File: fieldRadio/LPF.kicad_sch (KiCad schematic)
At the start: 91 parts, among them K1 G5V-2, K2 G5V-2, K3 G5V-2, K4 G5V-2, K5 G5V-2, Q1 MMBT3904, Q2 MMBT3904, Q3 MMBT3904, Q4 MMBT3904, Q5 MMBT3904

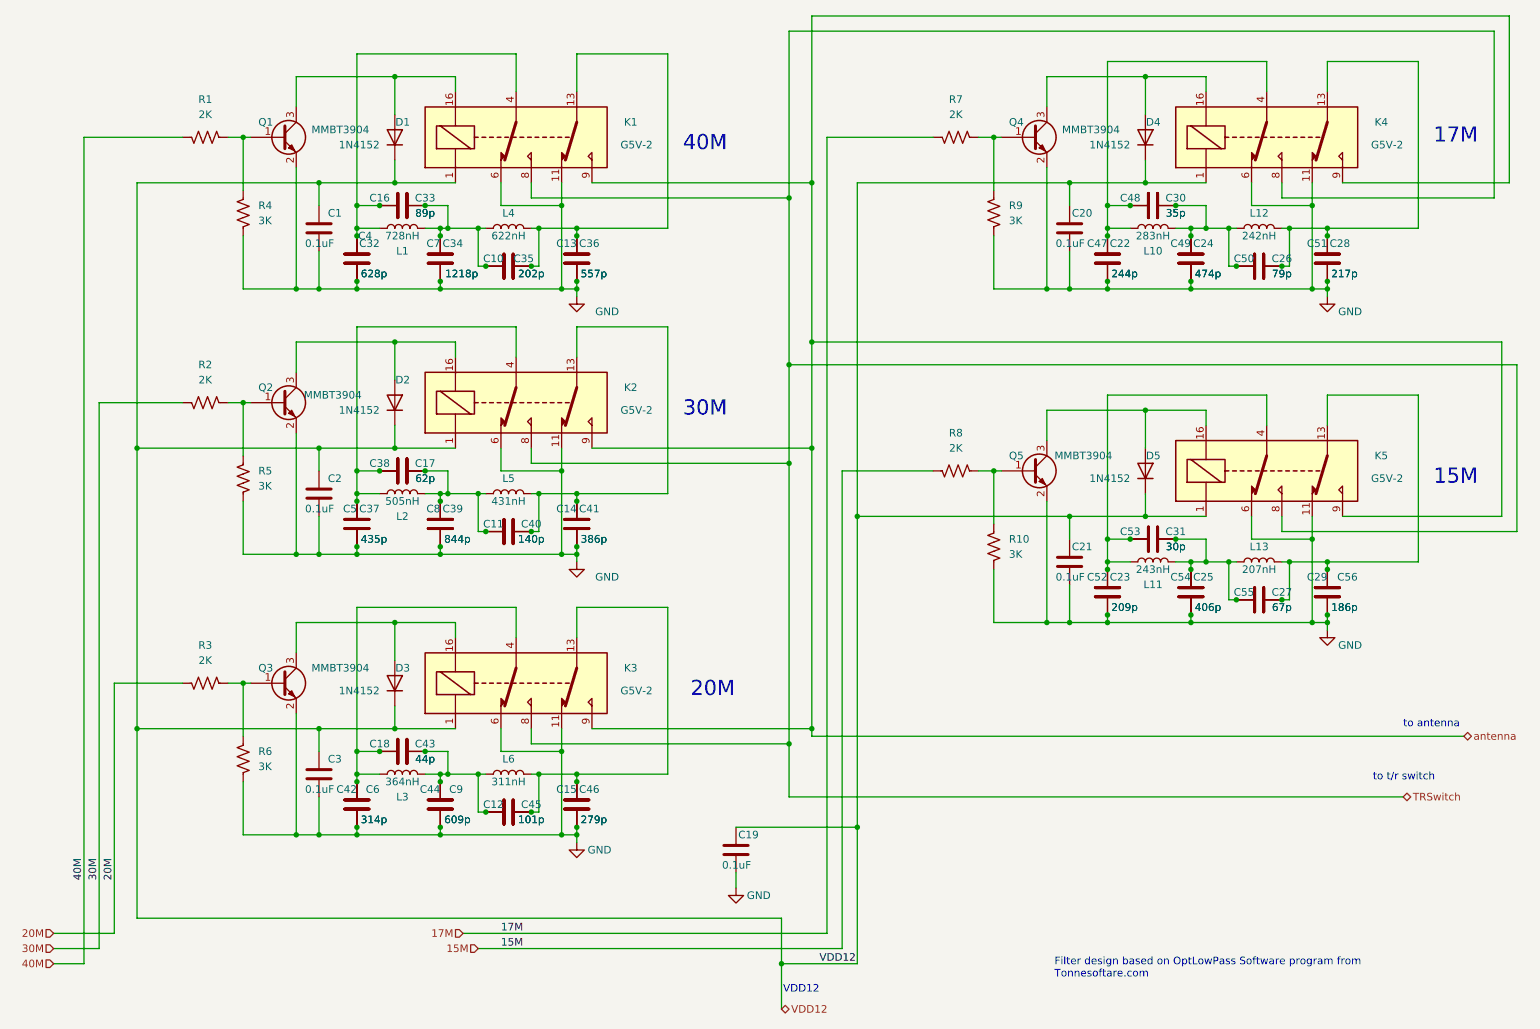
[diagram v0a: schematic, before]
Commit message: Building fieldradio schematic
in process of building field radio schematics
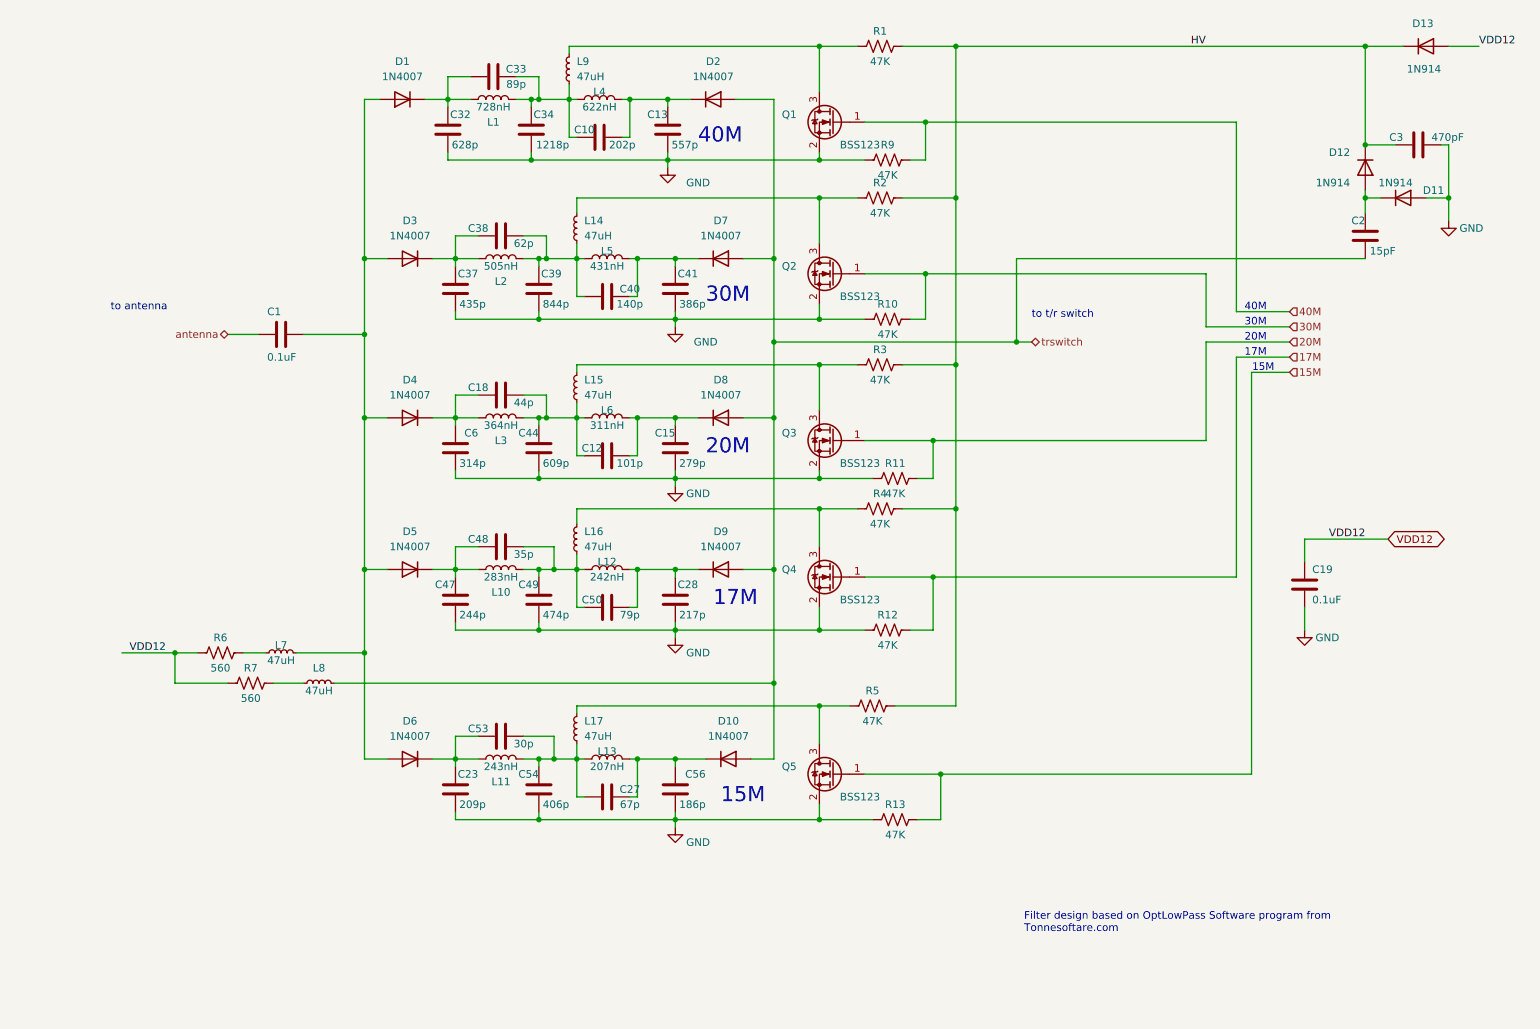
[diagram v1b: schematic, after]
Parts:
- removed C11: 140p, Capacitor_THT:C_Disc_D4.3mm_W1.9mm_P5.00mm, symbol Device:C
- removed C14: 386p, Capacitor_THT:C_Disc_D4.3mm_W1.9mm_P5.00mm, symbol Device:C
- removed C16: 89p, Capacitor_THT:C_Disc_D4.3mm_W1.9mm_P5.00mm, symbol Device:C
- removed C17: 62p, Capacitor_THT:C_Disc_D4.3mm_W1.9mm_P5.00mm, symbol Device:C
- removed C20, C21: 0.1uF, Capacitor_SMD:C_0603_1608Metric_Pad1.08x0.95mm_HandSolder, symbol Device:C
- removed C22: 244p, Capacitor_THT:C_Disc_D4.3mm_W1.9mm_P5.00mm, symbol Device:C
- removed C24: 474p, Capacitor_THT:C_Disc_D4.3mm_W1.9mm_P5.00mm, symbol Device:C
- removed C25: 406p, Capacitor_THT:C_Disc_D4.3mm_W1.9mm_P5.00mm, symbol Device:C
- removed C26: 79p, Capacitor_THT:C_Disc_D4.3mm_W1.9mm_P5.00mm, symbol Device:C
- removed C29: 186p, Capacitor_THT:C_Disc_D4.3mm_W1.9mm_P5.00mm, symbol Device:C
- removed C30: 35p, Capacitor_THT:C_Disc_D4.3mm_W1.9mm_P5.00mm, symbol Device:C
- removed C31: 30p, Capacitor_THT:C_Disc_D4.3mm_W1.9mm_P5.00mm, symbol Device:C
- removed C35: 202p, Capacitor_THT:C_Disc_D4.3mm_W1.9mm_P5.00mm, symbol Device:C
- removed C36: 557p, Capacitor_THT:C_Disc_D4.3mm_W1.9mm_P5.00mm, symbol Device:C
- removed C4: 628p, Capacitor_THT:C_Disc_D4.3mm_W1.9mm_P5.00mm, symbol Device:C
- removed C42: 314p, Capacitor_THT:C_Disc_D4.3mm_W1.9mm_P5.00mm, symbol Device:C
- removed C43: 44p, Capacitor_THT:C_Disc_D4.3mm_W1.9mm_P5.00mm, symbol Device:C
- removed C45: 101p, Capacitor_THT:C_Disc_D4.3mm_W1.9mm_P5.00mm, symbol Device:C
- removed C46: 279p, Capacitor_THT:C_Disc_D4.3mm_W1.9mm_P5.00mm, symbol Device:C
- removed C5: 435p, Capacitor_THT:C_Disc_D4.3mm_W1.9mm_P5.00mm, symbol Device:C
- removed C51: 217p, Capacitor_THT:C_Disc_D4.3mm_W1.9mm_P5.00mm, symbol Device:C
- removed C52: 209p, Capacitor_THT:C_Disc_D4.3mm_W1.9mm_P5.00mm, symbol Device:C
- removed C55: 67p, Capacitor_THT:C_Disc_D4.3mm_W1.9mm_P5.00mm, symbol Device:C
- removed C7: 1218p, Capacitor_THT:C_Disc_D4.3mm_W1.9mm_P5.00mm, symbol Device:C
- removed C8: 844p, Capacitor_THT:C_Disc_D4.3mm_W1.9mm_P5.00mm, symbol Device:C
- removed C9: 609p, Capacitor_THT:C_Disc_D4.3mm_W1.9mm_P5.00mm, symbol Device:C
- removed D1, D2, D3, D4, D5: 1N4152, Diode_THT:D_DO-41_SOD81_P7.62mm_Horizontal, symbol Device:D
- removed K1, K2, K3, K4, K5: G5V-2, Relay_THT:Relay_DPDT_Omron_G5V-2, symbol Relay:G5V-2
- removed Q1, Q2, Q3, Q4, Q5: MMBT3904, Package_TO_SOT_SMD:SOT-23, symbol Device:Q_NPN_BEC
- removed R8: 2K, Resistor_SMD:R_0603_1608Metric_Pad0.98x0.95mm_HandSolder, symbol Device:R_US
- added D1, D10, D2, D3, D4, D5, D6, D7, D8, D9: 1N4007, Diode_THT:D_DO-41_SOD81_P10.16mm_Horizontal, symbol Diode:1N4007
- added D11, D12, D13: 1N914, Diode_THT:D_DO-35_SOD27_P7.62mm_Horizontal, symbol Diode:1N914
- added L14, L15, L16, L17, L7, L8, L9: 47uH, Inductor_THT:L_Axial_L11.0mm_D4.5mm_P7.62mm_Vertical_Fastron_MECC, symbol Device:L_Small
- added Q1, Q2, Q3, Q4, Q5: BSS123, Package_TO_SOT_SMD:SOT-23-3, symbol Device:Q_NMOS_GSD
- added R11, R12, R13: 47K, Resistor_SMD:R_0603_1608Metric_Pad0.98x0.95mm_HandSolder, symbol Device:R_US
- C1: footprint Capacitor_SMD:C_0603_1608Metric_Pad1.08x0.95mm_HandSolder -> Capacitor_THT:C_Disc_D4.3mm_W1.9mm_P5.00mm
- C10, C12, C13, C15, C18, C23, C27, C28, C32, C33, C34, C37, C38, C39, C40, C41, C44, C47, C48, C49, C50, C53, C54, C56, C6: footprint Capacitor_THT:C_Disc_D4.3mm_W1.9mm_P5.00mm -> Capacitor_SMD:C_1206_3216Metric_Pad1.33x1.80mm_HandSolder
- C2: value 0.1uF -> 15pF; footprint Capacitor_SMD:C_0603_1608Metric_Pad1.08x0.95mm_HandSolder -> Capacitor_THT:C_Disc_D4.3mm_W1.9mm_P5.00mm
- C3: value 0.1uF -> 470pF; footprint Capacitor_SMD:C_0603_1608Metric_Pad1.08x0.95mm_HandSolder -> Capacitor_THT:C_Disc_D4.3mm_W1.9mm_P5.00mm
- R1, R2, R3: value 2K -> 47K
- R10, R4, R5, R9: value 3K -> 47K
- R6: value 3K -> 560; footprint Resistor_SMD:R_0603_1608Metric_Pad0.98x0.95mm_HandSolder -> Resistor_THT:R_Axial_DIN0617_L17.0mm_D6.0mm_P20.32mm_Horizontal
- R7: value 2K -> 560; footprint Resistor_SMD:R_0603_1608Metric_Pad0.98x0.95mm_HandSolder -> Resistor_THT:R_Axial_DIN0617_L17.0mm_D6.0mm_P20.32mm_Horizontal
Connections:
- net 15M: now also Q5.1 (G), R13.2
- net 17M: now also Q4.1 (G), R12.2; no longer R7.2
- net 20M: now also Q3.1 (G), R11.2; no longer R3.2
- net 30M: now also R10.2, Q2.1 (G); no longer R2.2
- net 40M: now also R9.2, Q1.1 (G); no longer R1.2
- net GND: now also C19.1, R10.1, R9.1, D11.2 (A), Q1.2 (S), Q2.2 (S), Q3.2 (S), Q4.2 (S), Q5.2 (S), R11.1, R12.1, R13.1; no longer C1.2, C19.2, C2.2, R10.2, R4.2, R5.2, R6.2, R9.2
- net VDD12: now also C19.2, R6.1, R7.1, D13.2 (A); no longer C1.1, C19.1, C2.1, C3.1
- net antenna: now also C1.1
- net at C12.2, C18.1, C44.1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: now also L15.1
- net at C40.1, C41.1, L5.1: now also D7.1 (K)
- net at C38.1, C39.1, C40.2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: now also L14.1
- net at R3.1: now also L15.2, Q3.3 (D); no longer R6.1
- net at C27.2, C53.1, C54.1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: now also L17.1
- net at C23.1, C53.2, L11.2: now also D6.1 (K)
- net at C12.1, C15.1, L6.1: now also D8.1 (K)
- net at C18.2, C6.1, L3.2: now also D4.1 (K)
- net at C37.1, C38.2, L2.2: now also D3.1 (K)
- net at C27.1, C56.1, L13.1: now also D10.1 (K)
- net at C10.1, C13.1, L4.1: now also D2.1 (K)
- net at C10.2, C33.1, C34.1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: now also L9.1
- net at R4.1: now also L16.2, Q4.3 (D); no longer R1.1
- net at C32.1, C33.2, L1.2: now also D1.1 (K)
- net at C47.1, C48.2, L10.2: now also D5.1 (K)
- net at C28.1, C50.1, L12.1: now also D9.1 (K)
- net at R5.1: now also L17.2, Q5.3 (D); no longer R2.1
- net at C48.1, C49.1, C50.2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: now also L16.1
- new net: C1.2, D1.2 (A), D3.2 (A), D4.2 (A), D5.2 (A), D6.2 (A), L7.2
- new net: L8.1, R7.2
- new net: C2.1, D11.1 (K), D12.2 (A)
- new net: L14.2, Q2.3 (D), R2.1
- new net: L9.2, Q1.3 (D), R1.1
- new net: L7.1, R6.2
- new net HV: C3.1, D12.1 (K), D13.1 (K), R1.2, R2.2, R3.2, R4.2, R5.2
- new net trswitch: C2.2, D10.2 (A), D2.2 (A), D7.2 (A), D8.2 (A), D9.2 (A), L8.2
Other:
- note removed: "VDD12"
- moved on the sheet: C10, C12, C13, C15, C18, C19, C23, C27, C28, C32, C33, C34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

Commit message: More schematic dev.
More schematic development
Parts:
- renumbered C37 to C10, C6 to C11, C47 to C12, C23 to C13, C33 to C14, C38 to C15, C18 to C16, C48 to C17, C53 to C18, C34 to C19, C39 to C20, C44 to C21, C49 to C22, C54 to C23, C10 to C24, C40 to C25, C12 to C26, C50 to C27, C27 to C28, C13 to C29, C41 to C30, C15 to C31, C28 to C32, C56 to C33, C19 to C34, C2 to C35, C3 to C36, C1 to C8, C32 to C9, D6 to D10, D2 to D11, D7 to D12, D8 to D13, D9 to D14, D10 to D15, D12 to D16, D11 to D17, D13 to D18, D1 to D6, D3 to D7, D4 to D8, D5 to D9, L9 to L12, L14 to L13, L15 to L14, L16 to L15, L17 to L16, L4 to L17, L5 to L18, L6 to L19, L12 to L20, L13 to L21, L7 to L5, L8 to L6, L1 to L7, L2 to L8, L3 to L9, Q4 to Q10, Q5 to Q11, Q1 to Q7, Q2 to Q8, Q3 to Q9, R6 to R15, R7 to R16, R5 to R17, R1 to R18, R2 to R19, R3 to R20, R4 to R21, R9 to R22, R10 to R23, R12 to R24, R11 to R25, R13 to R26

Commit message: Clean Up
Schematic clean up in prep for layout
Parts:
- L12, L13, L14, L15, L16, L5, L6: footprint Inductor_THT:L_Axial_L11.0mm_D4.5mm_P7.62mm_Vertical_Fastron_MECC -> Inductor_THT:L_Axial_L13.0mm_D4.5mm_P15.24mm_Horizontal_Fastron_HCCC
- renumbered C8 to C10, C9 to C11, C10 to C12, C11 to C13, C12 to C14, C13 to C15, C14 to C16, C15 to C17, C16 to C18, C17 to C19, C18 to C20, C19 to C21, C20 to C22, C21 to C23, C22 to C24, C23 to C25, C24 to C26, C25 to C27, C26 to C28, C27 to C29, C28 to C30, C29 to C31, C30 to C32, C31 to C33, C32 to C34, C33 to C35, C34 to C36, C35 to C37, C36 to C38

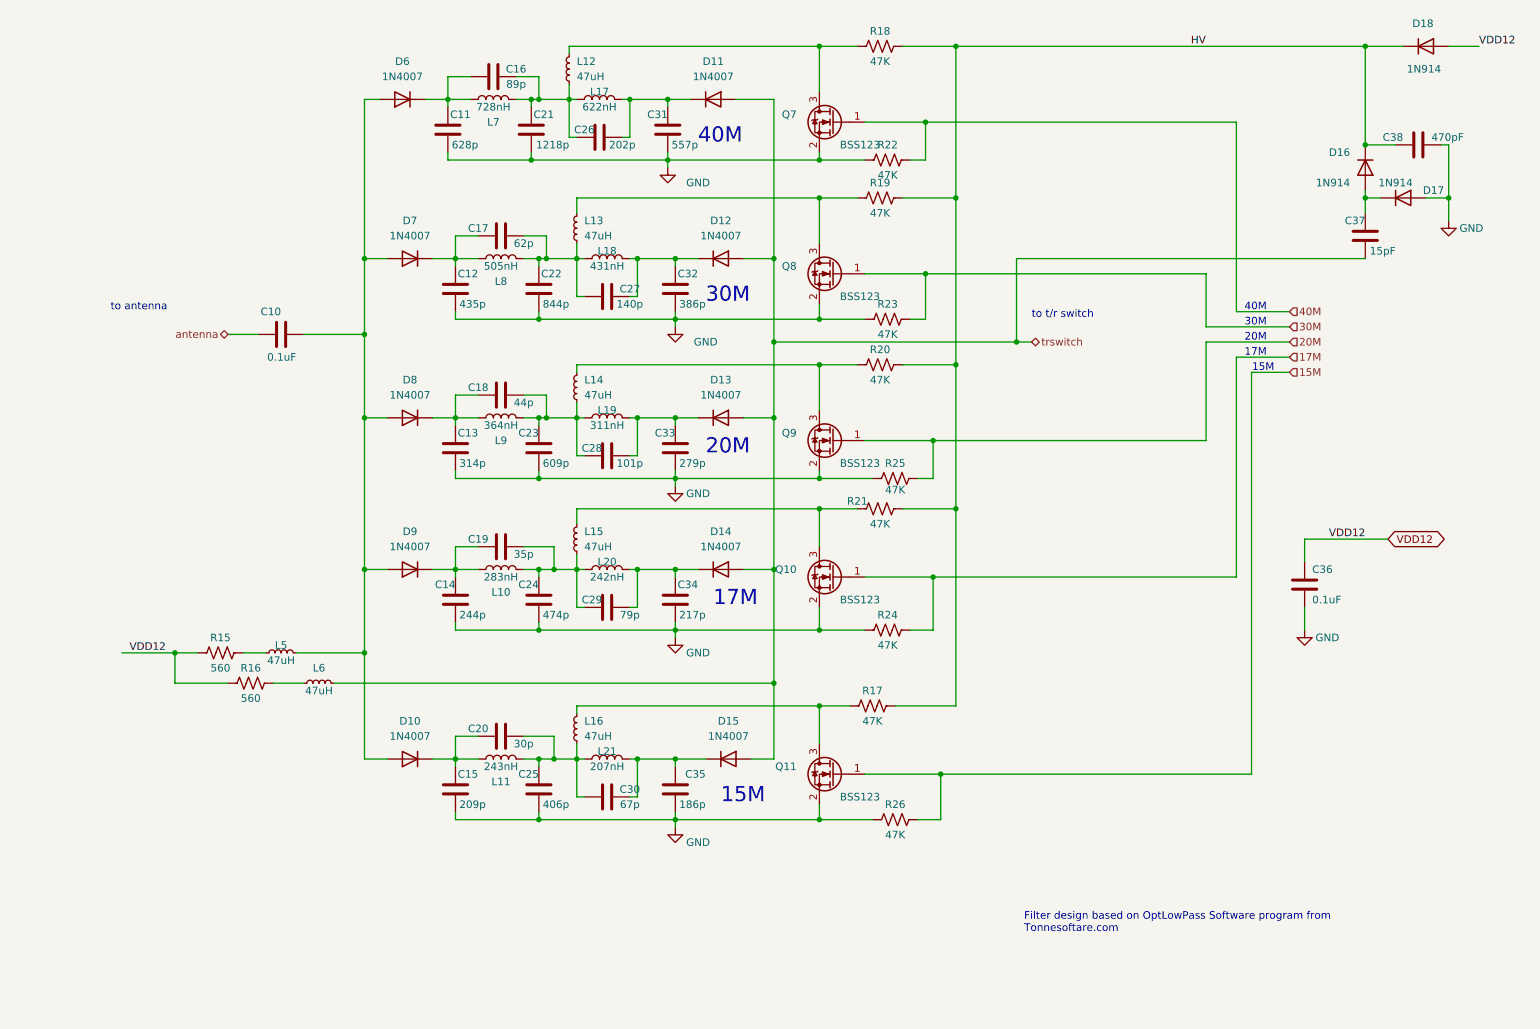
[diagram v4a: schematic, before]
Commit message: Placement of preselector and qsd
Finished placement of these two blocks
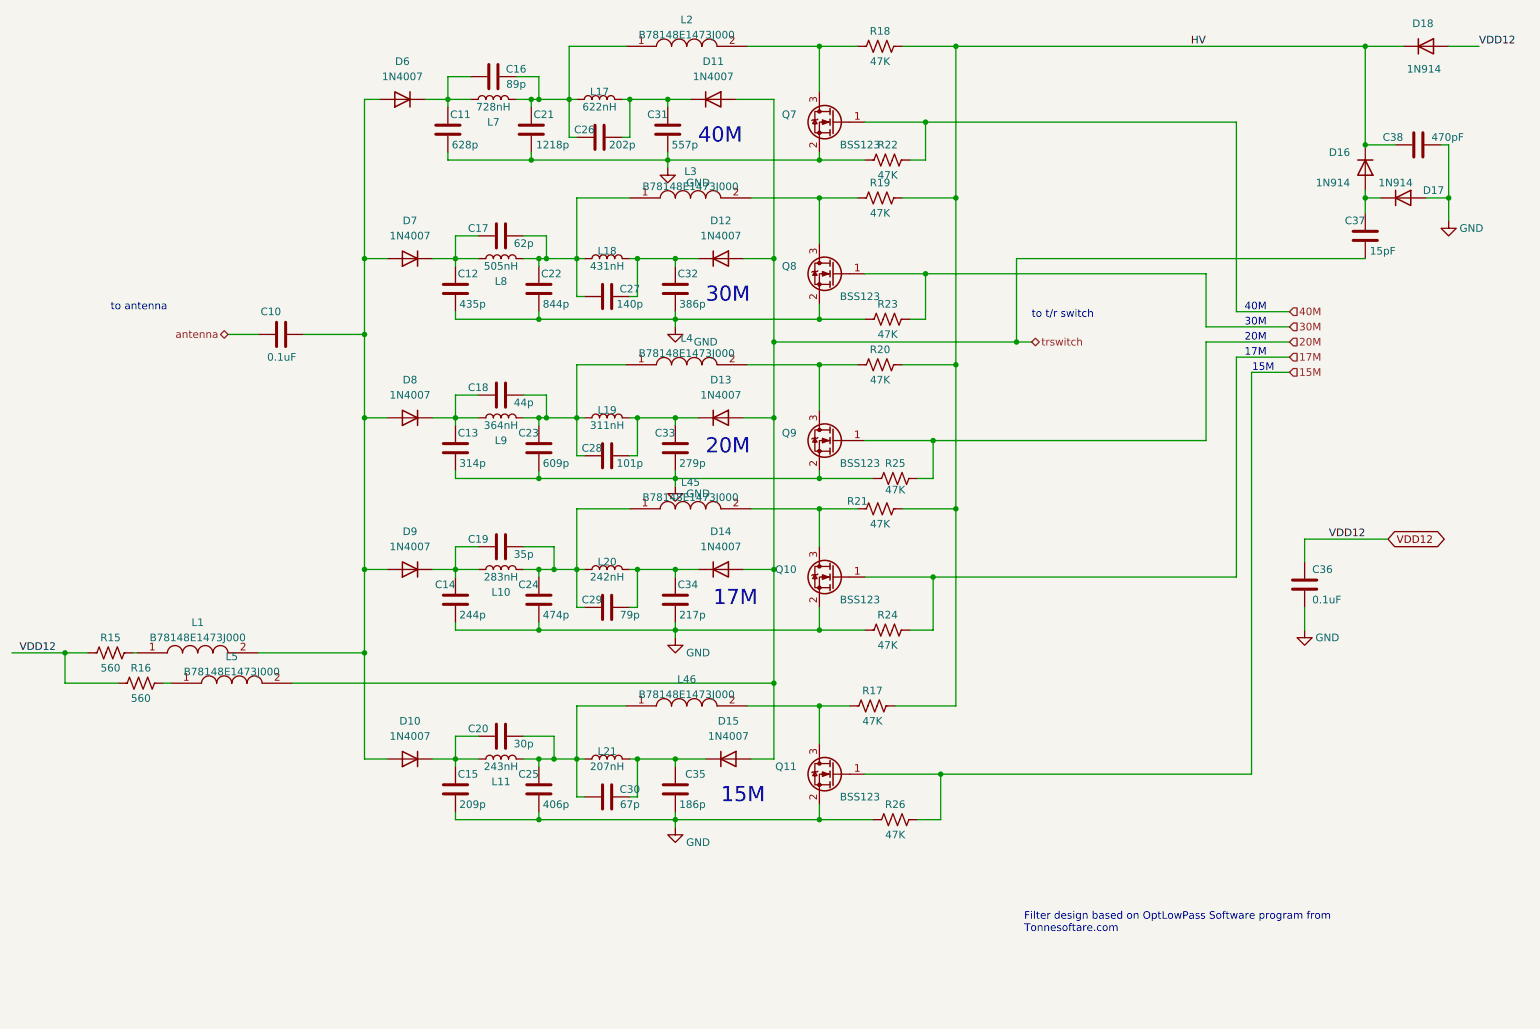
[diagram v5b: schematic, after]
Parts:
- removed L12, L13, L14, L15, L16, L5, L6: 47uH, Inductor_THT:L_Axial_L13.0mm_D4.5mm_P15.24mm_Horizontal_Fastron_HCCC, symbol Device:L_Small
- added L1, L2, L3, L4, L45, L46, L5: B78148E1473J000, B78148E, symbol SamacSys_Parts:B78148E1473J000
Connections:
- net trswitch: now also L5.2
- net at C10.2, D10.2 (A), D6.2 (A)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: now also L1.2
- net at Q10.3 (D), R21.1: now also L45.2
- net at C17.1, C22.1, C27.2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: now also L3.1
- net at R16.2: now also L5.1
- net at Q11.3 (D), R17.1: now also L46.2
- net at Q9.3 (D), R20.1: now also L4.2
- net at C19.1, C24.1, C29.2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: now also L45.1
- net at C16.1, C21.1, C26.2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: now also L2.1
- net at C20.1, C25.1, C30.2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: now also L46.1
- net at Q8.3 (D), R19.1: now also L3.2
- net at Q7.3 (D), R18.1: now also L2.2
- net at C18.1, C23.1, C28.2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: now also L4.1
- net at R15.2: now also L1.1
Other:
- moved on the sheet: R15, R16

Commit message: Added support for unused gpio
Also added option for external clock generator.
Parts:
- R15, R16: footprint Resistor_THT:R_Axial_DIN0617_L17.0mm_D6.0mm_P20.32mm_Horizontal -> Resistor_THT:R_Axial_DIN0207_L6.3mm_D2.5mm_P10.16mm_Horizontal
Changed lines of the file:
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@@
       (effects (font (size 1.27 1.27)))
     )
-    (property "Footprint" "Resistor_THT:R_Axial_DIN0617_L17.0mm_D6.0mm_P20.32mm_Horizontal" (at 103.759 153.924 90)
+    (property "Footprint" "Resistor_THT:R_Axial_DIN0207_L6.3mm_D2.5mm_P10.16mm_Horizontal" (at 103.759 153.924 90)
       (effects (font (size 1.27 1.27)) hide)
     )
@@
       (effects (font (size 1.27 1.27)))
     )
-    (property "Footprint" "Resistor_THT:R_Axial_DIN0617_L17.0mm_D6.0mm_P20.32mm_Horizontal" (at 98.679 148.844 90)
-      (effects (font (size 1.27 1.27)) hide)
-    )
+    (property "Footprint" "Resistor_THT:R_Axial_DIN0207_L6.3mm_D2.5mm_P10.16mm_Horizontal" (at 98.679 148.844 90)
+      (effects (font (size 1.27 1.27)) hide)
+    )
